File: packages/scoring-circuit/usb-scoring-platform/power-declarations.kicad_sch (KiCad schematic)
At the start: 0 parts

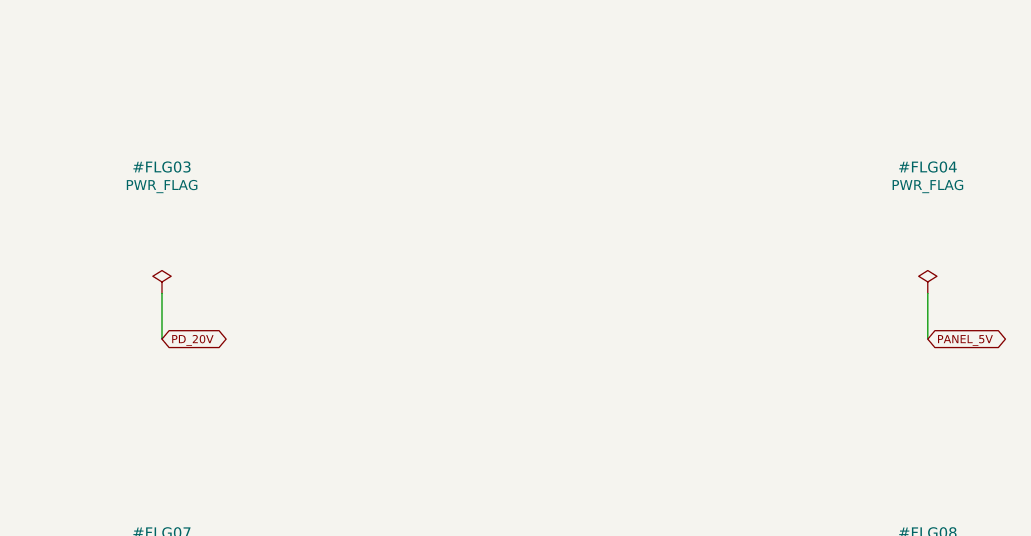
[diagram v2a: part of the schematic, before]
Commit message: feat(scoring-circuit): replace dual USB inputs with shared isolated power design
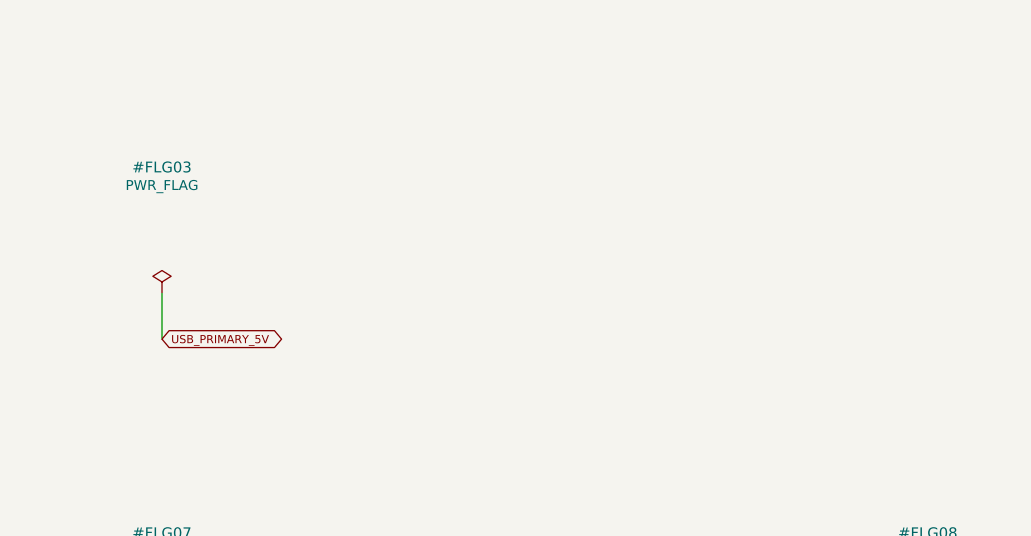
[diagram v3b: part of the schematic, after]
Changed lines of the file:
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@@
+(kicad_sch (version 20250114)
+(generator "eeschema")
+(paper "A3")
+(title_block (title "Power source declarations and design status") (rev "Engineering draft") (comment 1 "NOT FOR FABRICATION"))
+(symbol (lib_id "power:PWR_FLAG") (at 54.61 44.45 0) (unit 1) (in_bom yes) (on_board yes) (dnp no) (property "Reference" "#FLG01" (at 54.61 30.45 0) (effects (font (size 1.2 1.2)))) (property "Value" "PWR_FLAG" (at 54.61 32.45 0) (effects (font (size 1.1 1.1)))) (property "Footprint" "" (at 54.61 44.45 0) (effects (font (size 1 1)) (hide yes))) (pin "1") (instances (project "usb-scoring-platform" (path "/20cc8167-128c-446a-a106-f942323e143f/6015af84-8930-4c68-ae3a-f26aec9e5809" (reference "#FLG01") (unit 1)))))
+(wire (pts (xy 54.61 44.45) (xy 54.61 49.53)) (stroke (width 0) (type default)))
+(global_label "GND" (shape bidirectional) (at 54.61 49.53 0) (effects (font (size 0.9 0.9)) (justify left)) (property "Intersheetrefs" "" (at 54.61 49.53 0) (effects (font (size 1 1)) (hide yes))))
+(symbol (lib_id "power:PWR_FLAG") (at 139.7 44.45 0) (unit 1) (in_bom yes) (on_board yes) (dnp no) (property "Reference" "#FLG02" (at 139.7 30.45 0) (effects (font (size 1.2 1.2)))) (property "Value" "PWR_FLAG" (at 139.7 32.45 0) (effects (font (size 1.1 1.1)))) (property "Footprint" "" (at 139.7 44.45 0) (effects (font (size 1 1)) (hide yes))) (pin "1") (instances (project "usb-scoring-platform" (path "/20cc8167-128c-446a-a106-f942323e143f/6015af84-8930-4c68-ae3a-f26aec9e5809" (reference "#FLG02") (unit 1)))))
+(wire (pts (xy 139.7 44.45) (xy 139.7 49.53)) (stroke (width 0) (type default)))
+(global_label "USB_VBUS" (shape bidirectional) (at 139.7 49.53 0) (effects (font (size 0.9 0.9)) (justify left)) (property "Intersheetrefs" "" (at 139.7 49.53 0) (effects (font (size 1 1)) (hide yes))))
+(symbol (lib_id "power:PWR_FLAG") (at 224.79 44.45 0) (unit 1) (in_bom yes) (on_board yes) (dnp no) (property "Reference" "#FLG03" (at 224.79 30.45 0) (effects (font (size 1.2 1.2)))) (property "Value" "PWR_FLAG" (at 224.79 32.45 0) (effects (font (size 1.1 1.1)))) (property "Footprint" "" (at 224.79 44.45 0) (effects (font (size 1 1)) (hide yes))) (pin "1") (instances (project "usb-scoring-platform" (path "/20cc8167-128c-446a-a106-f942323e143f/6015af84-8930-4c68-ae3a-f26aec9e5809" (reference "#FLG03") (unit 1)))))
+(wire (pts (xy 224.79 44.45) (xy 224.79 49.53)) (stroke (width 0) (type default)))
+(global_label "USB_PRIMARY_5V" (shape bidirectional) (at 224.79 49.53 0) (effects (font (size 0.9 0.9)) (justify left)) (property "Intersheetrefs" "" (at 224.79 49.53 0) (effects (font (size 1 1)) (hide yes))))
+(symbol (lib_id "power:PWR_FLAG") (at 54.61 85.09 0) (unit 1) (in_bom yes) (on_board yes) (dnp no) (property "Reference" "#FLG05" (at 54.61 71.09 0) (effects (font (size 1.2 1.2)))) (property "Value" "PWR_FLAG" (at 54.61 73.09 0) (effects (font (size 1.1 1.1)))) (property "Footprint" "" (at 54.61 85.09 0) (effects (font (size 1 1)) (hide yes))) (pin "1") (instances (project "usb-scoring-platform" (path "/20cc8167-128c-446a-a106-f942323e143f/6015af84-8930-4c68-ae3a-f26aec9e5809" (reference "#FLG05") (unit 1)))))
+(wire (pts (xy 54.61 85.09) (xy 54.61 90.17)) (stroke (width 0) (type default)))
+(global_label "CORE_5V" (shape bidirectional) (at 54.61 90.17 0) (effects (font (size 0.9 0.9)) (justify left)) (property "Intersheetrefs" "" (at 54.61 90.17 0) (effects (font (size 1 1)) (hide yes))))
+(symbol (lib_id "power:PWR_FLAG") (at 139.7 85.09 0) (unit 1) (in_bom yes) (on_board yes) (dnp no) (property "Reference" "#FLG06" (at 139.7 71.09 0) (effects (font (size 1.2 1.2)))) (property "Value" "PWR_FLAG" (at 139.7 73.09 0) (effects (font (size 1.1 1.1)))) (property "Footprint" "" (at 139.7 85.09 0) (effects (font (size 1 1)) (hide yes))) (pin "1") (instances (project "usb-scoring-platform" (path "/20cc8167-128c-446a-a106-f942323e143f/6015af84-8930-4c68-ae3a-f26aec9e5809" (reference "#FLG06") (unit 1)))))
+(wire (pts (xy 139.7 85.09) (xy 139.7 90.17)) (stroke (width 0) (type default)))
+(global_label "APP_3V3" (shape bidirectional) (at 139.7 90.17 0) (effects (font (size 0.9 0.9)) (justify left)) (property "Intersheetrefs" "" (at 139.7 90.17 0) (effects (font (size 1 1)) (hide yes))))
+(symbol (lib_id "power:PWR_FLAG") (at 224.79 85.09 0) (unit 1) (in_bom yes) (on_board yes) (dnp no) (property "Reference" "#FLG07" (at 224.79 71.09 0) (effects (font (size 1.2 1.2)))) (property "Value" "PWR_FLAG" (at 224.79 73.09 0) (effects (font (size 1.1 1.1)))) (property "Footprint" "" (at 224.79 85.09 0) (effects (font (size 1 1)) (hide yes))) (pin "1") (instances (project "usb-scoring-platform" (path "/20cc8167-128c-446a-a106-f942323e143f/6015af84-8930-4c68-ae3a-f26aec9e5809" (reference "#FLG07") (unit 1)))))
+(wire (pts (xy 224.79 85.09) (xy 224.79 90.17)) (stroke (width 0) (type default)))
+(global_label "IR_3V3" (shape bidirectional) (at 224.79 90.17 0) (effects (font (size 0.9 0.9)) (justify left)) (property "Intersheetrefs" "" (at 224.79 90.17 0) (effects (font (size 1 1)) (hide yes))))
+(symbol (lib_id "power:PWR_FLAG") (at 309.88 85.09 0) (unit 1) (in_bom yes) (on_board yes) (dnp no) (property "Reference" "#FLG08" (at 309.88 71.09 0) (effects (font (size 1.2 1.2)))) (property "Value" "PWR_FLAG" (at 309.88 73.09 0) (effects (font (size 1.1 1.1)))) (property "Footprint" "" (at 309.88 85.09 0) (effects (font (size 1 1)) (hide yes))) (pin "1") (instances (project "usb-scoring-platform" (path "/20cc8167-128c-446a-a106-f942323e143f/6015af84-8930-4c68-ae3a-f26aec9e5809" (reference "#FLG08") (unit 1)))))
+(wire (pts (xy 309.88 85.09) (xy 309.88 90.17)) (stroke (width 0) (type default)))
+(global_label "USB_GND" (shape bidirectional) (at 309.88 90.17 0) (effects (font (size 0.9 0.9)) (justify left)) (property "Intersheetrefs" "" (at 309.88 90.17 0) (effects (font (size 1 1)) (hide yes))))
+(text "OPEN BEFORE FABRICATION" (at 30 170 0) (effects (font (size 2 2)) (justify left top)))
+(text "1. Conductor excitation/truth table and FIE thresholds; no patent-avoidance claim is established.\n2. External fault, ESD and power-off injection protection; USB component isolation is NOT complete board safety approval.\n3. USB enumeration/suspend/current and supply handover; power stability, capacitor derating and oscillator load.\n4. Complete placement, ground strategy, power routing, DRC, model alignment and bench acceptance.\n5. Exact HUB75 panel current and connector fit; FA-05 loop current/CTR, cable and polarity verification." (at 30 185 0) (effects (font (size 1.3 1.3)) (justify left top)))
+(text "Power source declarations and design status" (at 20 15 0) (effects (font (size 2 2)) (justify left top)))
+(text "Power flags describe external/module-fed nets for ERC only. They are not protection devices, proof of safety, or permission to fabricate." (at 20 22 0) (effects (font (size 0.95 0.95)) (justify left top)))
+(embedded_fonts no))

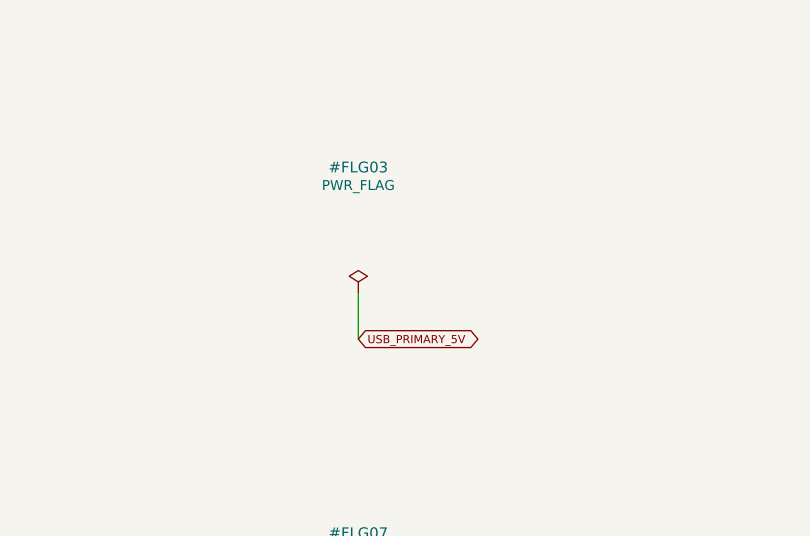
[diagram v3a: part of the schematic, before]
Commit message: fix(scoring-circuit): regulate isolated USB supply across input range
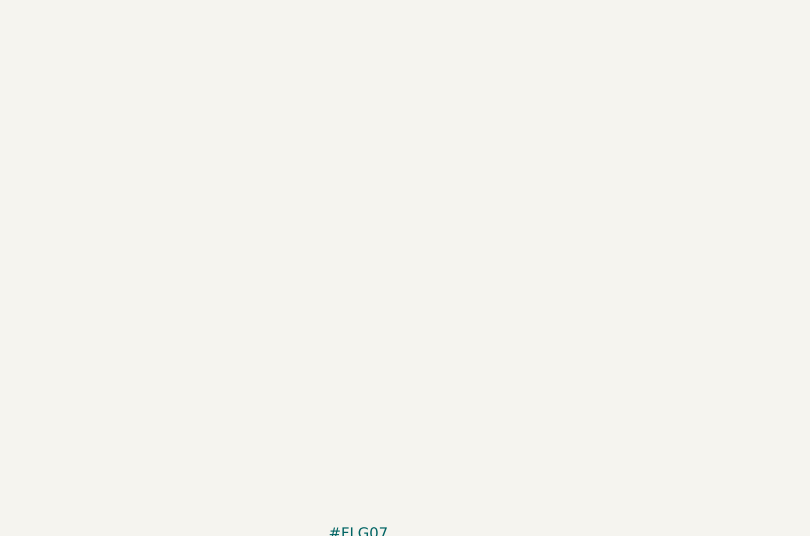
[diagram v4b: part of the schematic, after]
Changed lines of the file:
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@@
 (wire (pts (xy 139.7 44.45) (xy 139.7 49.53)) (stroke (width 0) (type default)))
 (global_label "USB_VBUS" (shape bidirectional) (at 139.7 49.53 0) (effects (font (size 0.9 0.9)) (justify left)) (property "Intersheetrefs" "" (at 139.7 49.53 0) (effects (font (size 1 1)) (hide yes))))
-(symbol (lib_id "power:PWR_FLAG") (at 224.79 44.45 0) (unit 1) (in_bom yes) (on_board yes) (dnp no) (property "Reference" "#FLG03" (at 224.79 30.45 0) (effects (font (size 1.2 1.2)))) (property "Value" "PWR_FLAG" (at 224.79 32.45 0) (effects (font (size 1.1 1.1)))) (property "Footprint" "" (at 224.79 44.45 0) (effects (font (size 1 1)) (hide yes))) (pin "1") (instances (project "usb-scoring-platform" (path "/20cc8167-128c-446a-a106-f942323e143f/6015af84-8930-4c68-ae3a-f26aec9e5809" (reference "#FLG03") (unit 1)))))
-(wire (pts (xy 224.79 44.45) (xy 224.79 49.53)) (stroke (width 0) (type default)))
-(global_label "USB_PRIMARY_5V" (shape bidirectional) (at 224.79 49.53 0) (effects (font (size 0.9 0.9)) (justify left)) (property "Intersheetrefs" "" (at 224.79 49.53 0) (effects (font (size 1 1)) (hide yes))))
 (symbol (lib_id "power:PWR_FLAG") (at 54.61 85.09 0) (unit 1) (in_bom yes) (on_board yes) (dnp no) (property "Reference" "#FLG05" (at 54.61 71.09 0) (effects (font (size 1.2 1.2)))) (property "Value" "PWR_FLAG" (at 54.61 73.09 0) (effects (font (size 1.1 1.1)))) (property "Footprint" "" (at 54.61 85.09 0) (effects (font (size 1 1)) (hide yes))) (pin "1") (instances (project "usb-scoring-platform" (path "/20cc8167-128c-446a-a106-f942323e143f/6015af84-8930-4c68-ae3a-f26aec9e5809" (reference "#FLG05") (unit 1)))))
 (wire (pts (xy 54.61 85.09) (xy 54.61 90.17)) (stroke (width 0) (type default)))
